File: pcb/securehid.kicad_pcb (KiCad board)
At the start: 2 copper layers, 129 x 69 mm, 200 parts, among them J1 USB_B_Micro, J2 SWD_HOST, J3 UART_HOST, J4 SWD_DEVICE, J5 UART_DEVICE, J6 USB_A, J7 USB_SPARE, J8 USB_A, Q1 AO3400, Q2 AO3400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

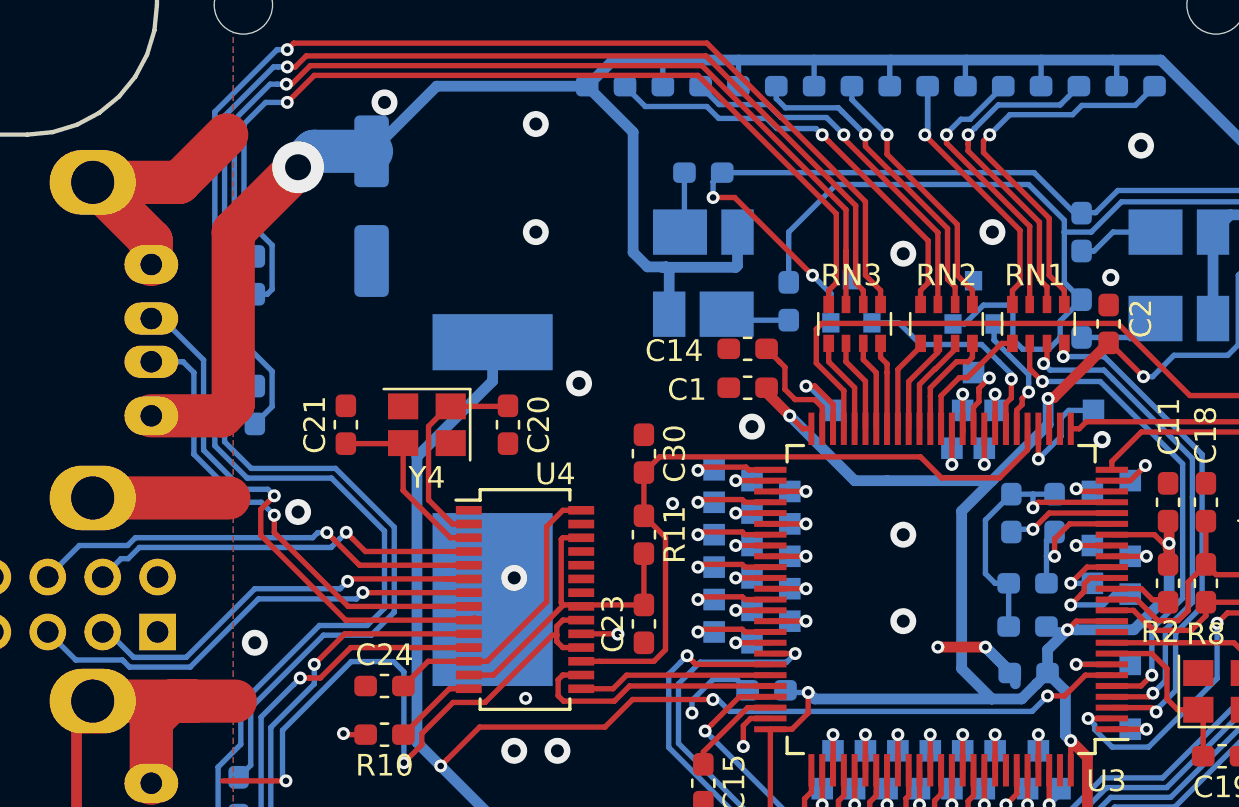
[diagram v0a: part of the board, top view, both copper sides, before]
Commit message: pcb: Add project info to silk and do gerber export
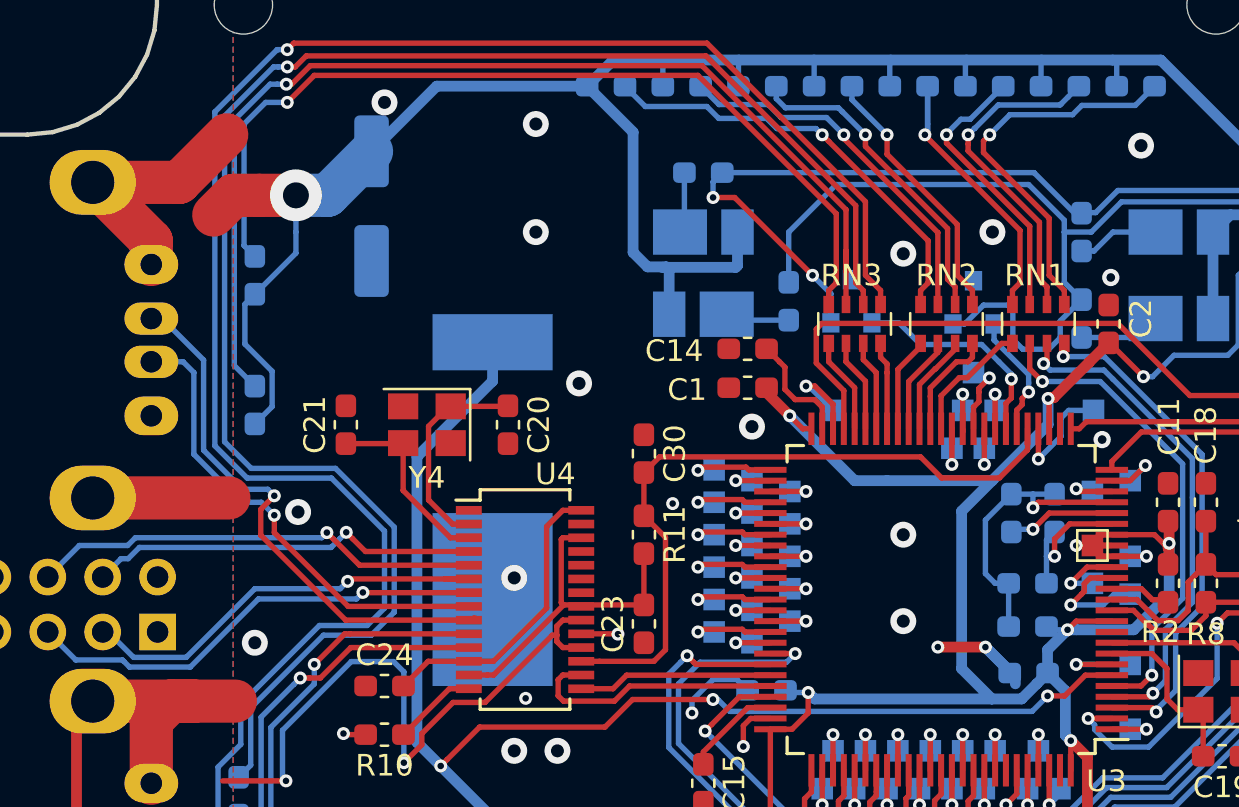
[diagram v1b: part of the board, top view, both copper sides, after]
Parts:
- TP58: moved to F.Cu
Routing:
- net VBUS: track 295.0 -> 281.3 mm
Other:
- board text added: "SecureHID v0.1 github.com/jaseg/securehid (c)2018 Jan GOETTE cc-by-sa"

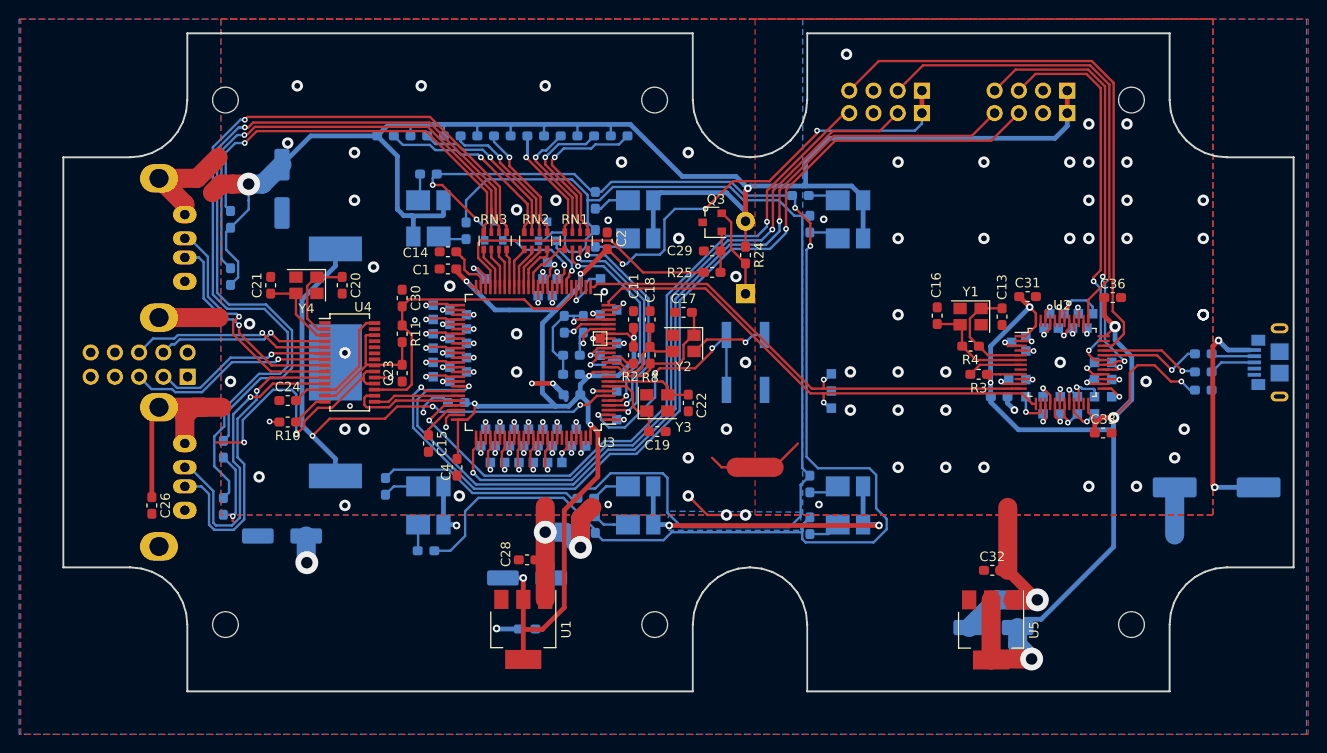
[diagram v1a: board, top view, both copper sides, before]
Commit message: Some small fixes, add silk artwork
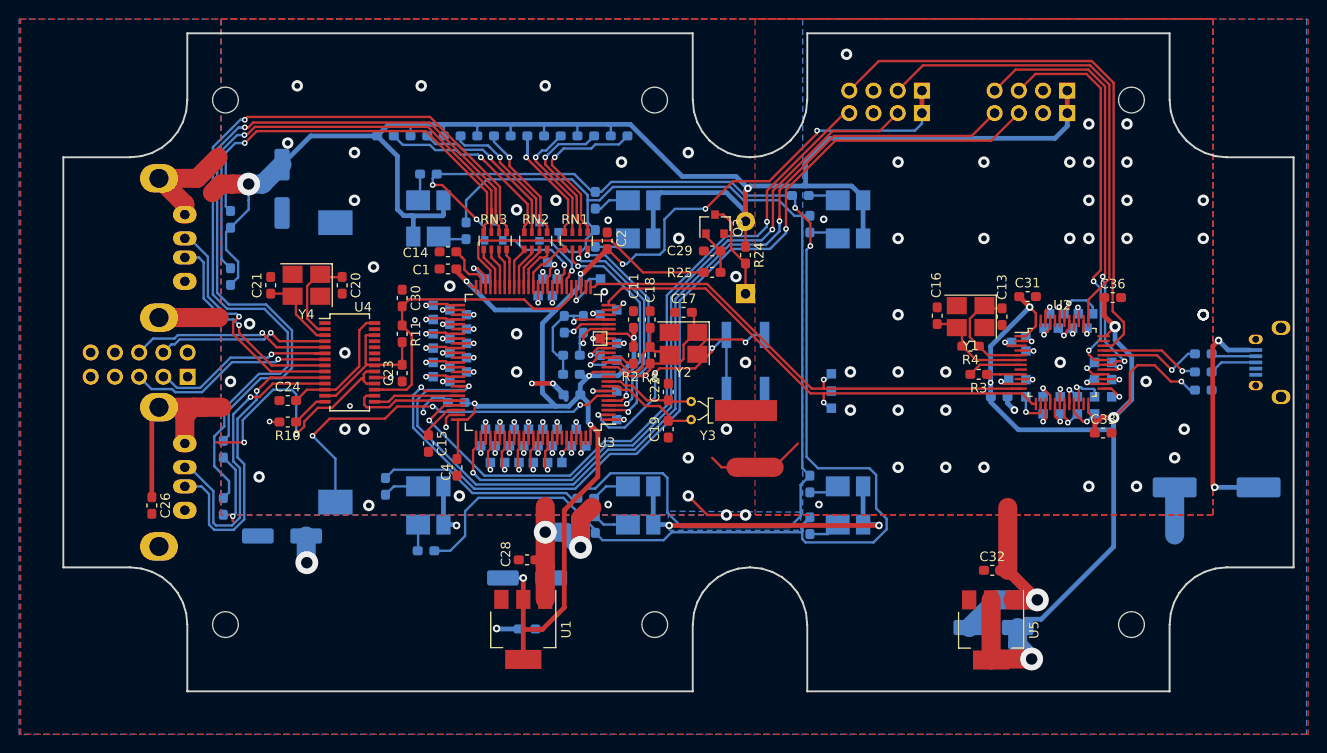
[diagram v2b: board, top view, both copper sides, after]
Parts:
- BT1: footprint Battery:BatteryHolder_MPD_BC2003_1x2032 -> Battery:BatteryHolder_Keystone_1060_1x2032
- J1: footprint Connector_USB:USB_Micro-B_GCT_USB3076-30-A -> footprints:microusb_ali_dovetail
- Y1, Y2, Y4: footprint Crystal:Crystal_SMD_TXC_7M-4Pin_3.2x2.5mm -> Crystal:Crystal_SMD_TXC_7M-4Pin_3.2x2.5mm_HandSoldering
- Y3: footprint Crystal:Crystal_SMD_TXC_7M-4Pin_3.2x2.5mm -> Crystal:Crystal_C26-LF_D2.1mm_L6.5mm_Horizontal_1EP_style1
- moved Y3 3.96 mm to (100.3, 87.0), turned to 90 degrees
- moved C22 2.39 mm to (97.9, 84.1), turned to 270 degrees
- moved J1 1.30 mm to (159.5, 81.0), turned to 90 degrees
- moved C19 1.18 mm to (97.9, 88.0), turned to 90 degrees
- moved Q3 0.35 mm to (102.8, 66.5), turned to 90 degrees
- moved Q1 0.16 mm to (85.4, 67.3), turned to 0 degrees
- turned BT1 to 90 degrees
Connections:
- Q1 pad 2: Net-(Q1-Pad2) -> GND
- Q1 pad 3: GND -> Net-(Q1-Pad3)
- Q3 pad 2: Net-(LS1-Pad1) -> GND
- Q3 pad 3: GND -> Net-(LS1-Pad1)
- R12 pad 2: Net-(Q1-Pad2) -> Net-(Q1-Pad3)
- R13 pad 2: Net-(Q1-Pad2) -> Net-(Q1-Pad3)
- R14 pad 2: Net-(Q1-Pad2) -> Net-(Q1-Pad3)
- R15 pad 2: Net-(Q1-Pad2) -> Net-(Q1-Pad3)
- R16 pad 2: Net-(Q1-Pad2) -> Net-(Q1-Pad3)
- R17 pad 2: Net-(Q1-Pad2) -> Net-(Q1-Pad3)
- Y3 pad 2: GND -> Net-(C22-Pad2)
- Y3 pad 3: Net-(C22-Pad2) -> GND
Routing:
- net Net-(Q1-Pad2): track 138.8 -> 0.00 mm
- net Net-(Q1-Pad3): track 0.00 -> 136.2 mm
- net Net-(BT1-Pad1): track 60.0 -> 41.2 mm
- net Net-(C19-Pad2): track 8.14 -> 10.6 mm
- net /ALARM_LED_BLUE: track 5.74 -> 7.10 mm
- net Net-(LS1-Pad1): track 9.50 -> 10.1 mm
- net Net-(C29-Pad1): track 4.35 -> 4.87 mm

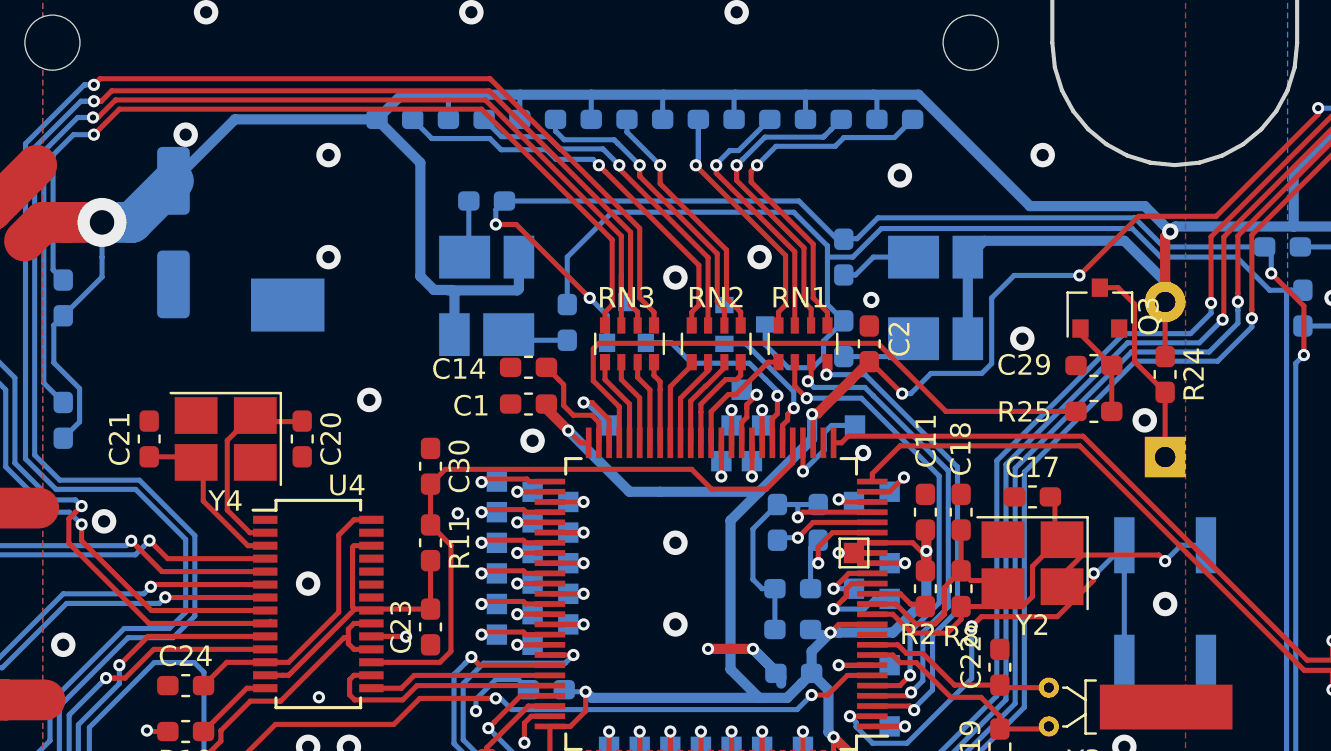
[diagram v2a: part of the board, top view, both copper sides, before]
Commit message: pcb: Fix a bunch of kicady layout errors
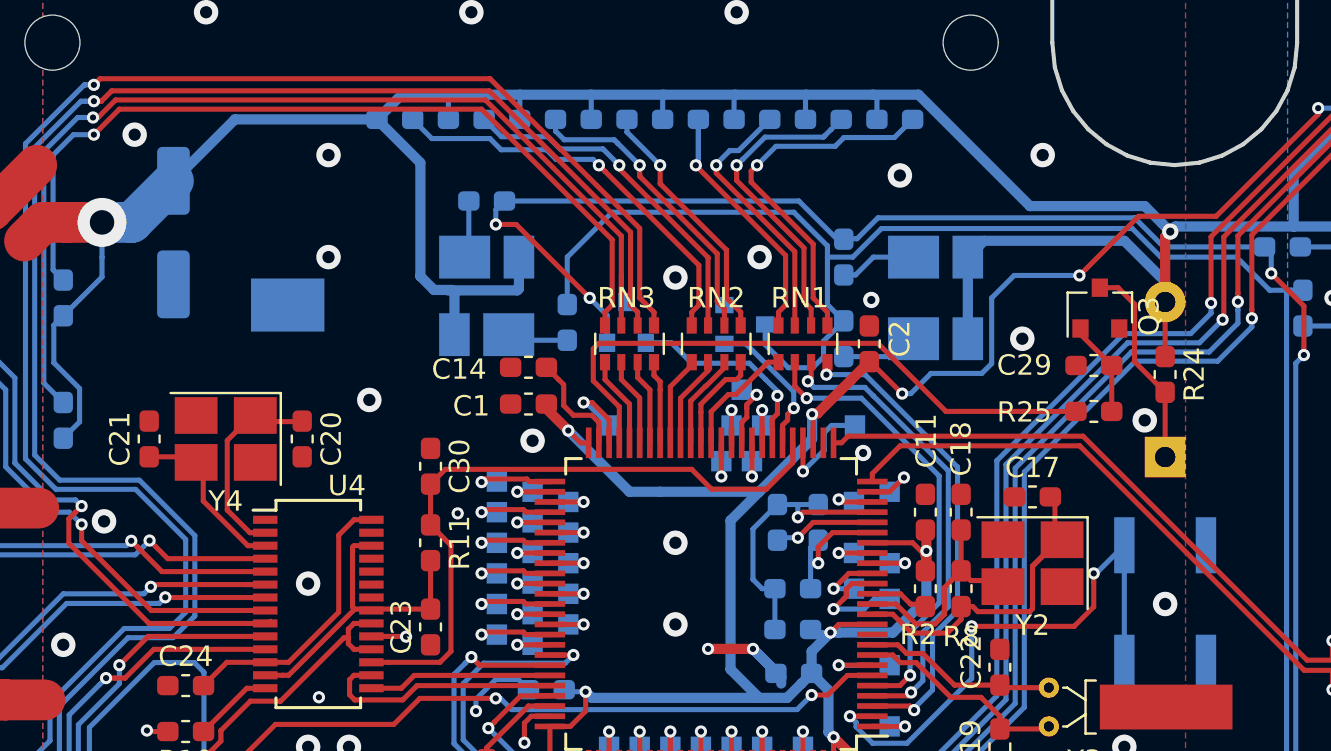
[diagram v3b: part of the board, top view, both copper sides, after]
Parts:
- TP58: moved to B.Cu
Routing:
- net GND: track 98.1 -> 89.9 mm, vias 43 -> 42
- net Net-(C17-Pad2): track 14.8 -> 17.4 mm
- net Net-(SW1-Pad2): track 26.7 -> 27.5 mm
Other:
- board text added: "SecureHID v0.2 github.com/jaseg/securehid (c)2018 Jan GOETTE cc-by-sa"
- board text removed: "SecureHID v0.1 github.com/jaseg/securehid (c)2018 Jan GOETTE cc-by-sa"

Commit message: Make a really fancy diagram
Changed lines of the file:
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@@
   (general
     (thickness 1.6)
-    (drawings 273)
+    (drawings 279)
     (tracks 1614)
     (zones 0)
@@
     )
   )
+  (gr_circle (center 134.5 76.5) (end 135 77) (layer F.SilkS) (width 0.2))
+  (gr_circle (center 62.5 76) (end 62 75.5) (layer F.SilkS) (width 0.2))
+  (gr_circle (center 80.5 78.5) (end 81 78.5) (layer F.SilkS) (width 0.2))
+  (gr_circle (center 80.5 78.5) (end 81 77.5) (layer F.SilkS) (width 0.2))
+  (gr_circle (center 87.5 84.5) (end 88 84) (layer F.SilkS) (width 0.2))
+  (gr_circle (center 93.5 88.5) (end 94 88) (layer F.SilkS) (width 0.2))
   (dimension 69 (width 0.3) (layer Cmts.User)
     (gr_text "69.000 mm" (at 20.4 81 270) (layer Cmts.User)
